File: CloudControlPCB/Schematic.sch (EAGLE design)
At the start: 19 parts, among them J1 AUDIO_JACK_TRRSSMD_RA, U1 LPC4088FBD208, U2 SGTL5000XNLA3R2, X1 PHB_1MM27_2X05_SNT

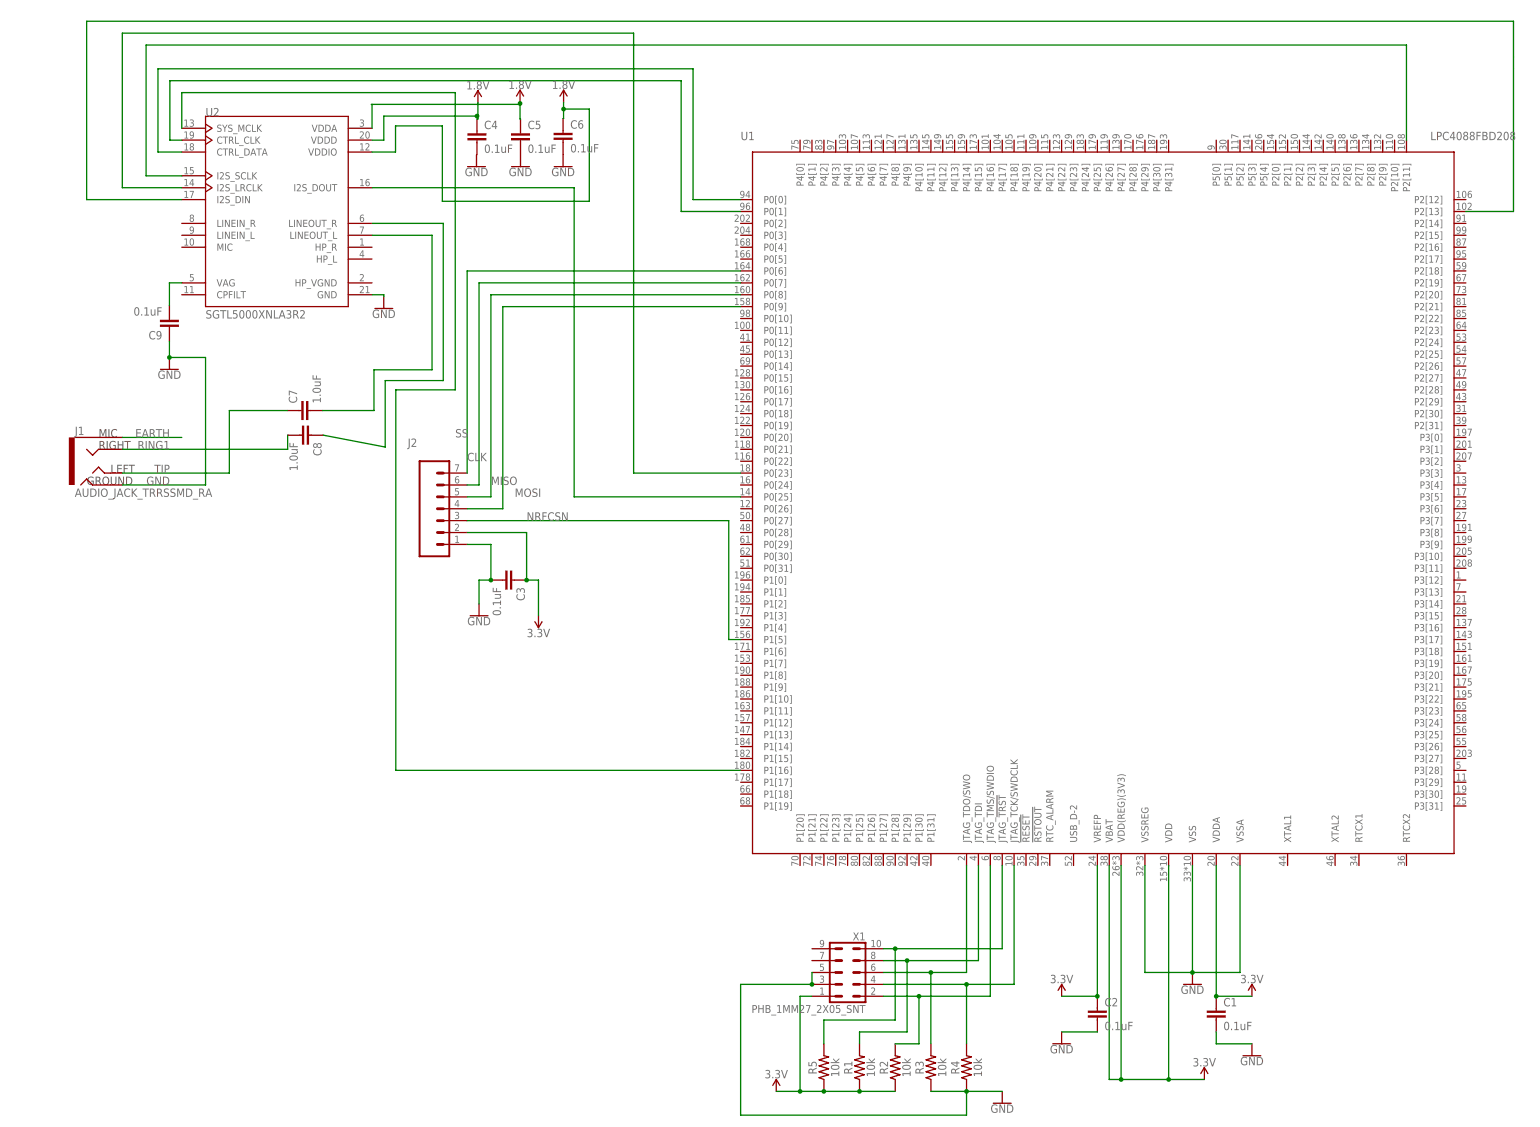
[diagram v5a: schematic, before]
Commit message: Fixed some wiring on the DAC
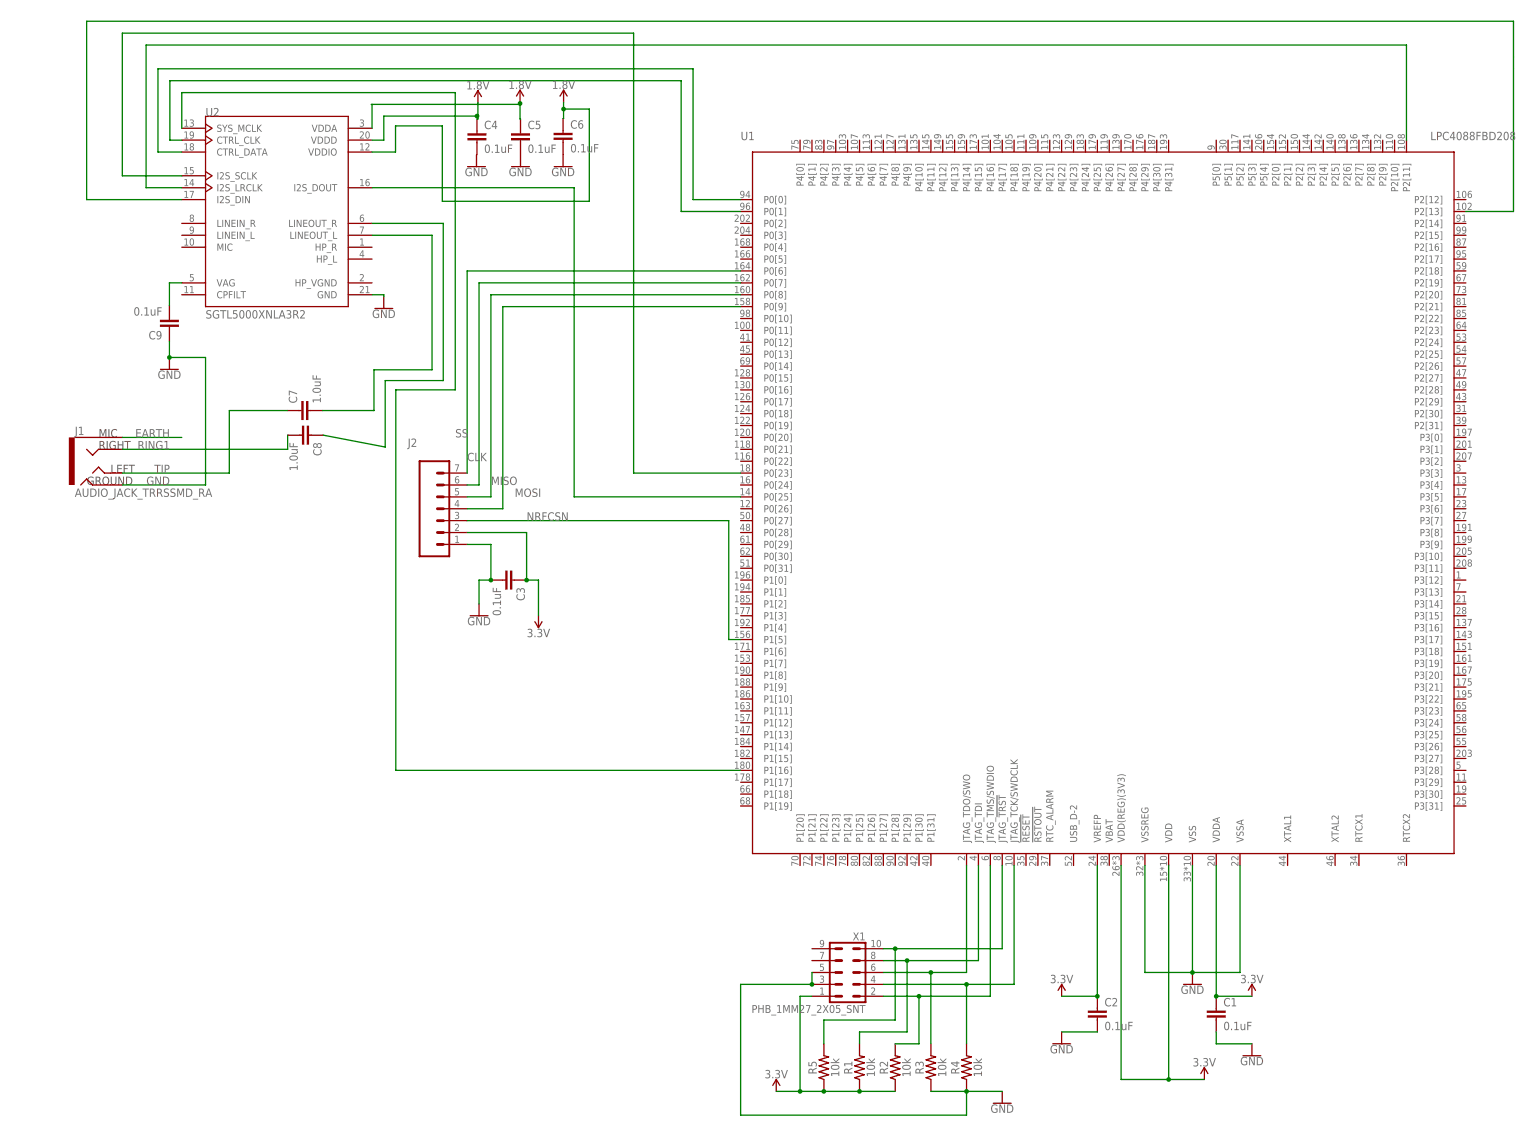
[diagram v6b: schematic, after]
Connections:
- net 3.3V: no longer U1.VBAT
- net N$10: now also U2.I2S_LRCLK; no longer U2.I2S_SCLK
- net N$11: now also U2.I2S_SCLK; no longer U2.I2S_LRCLK

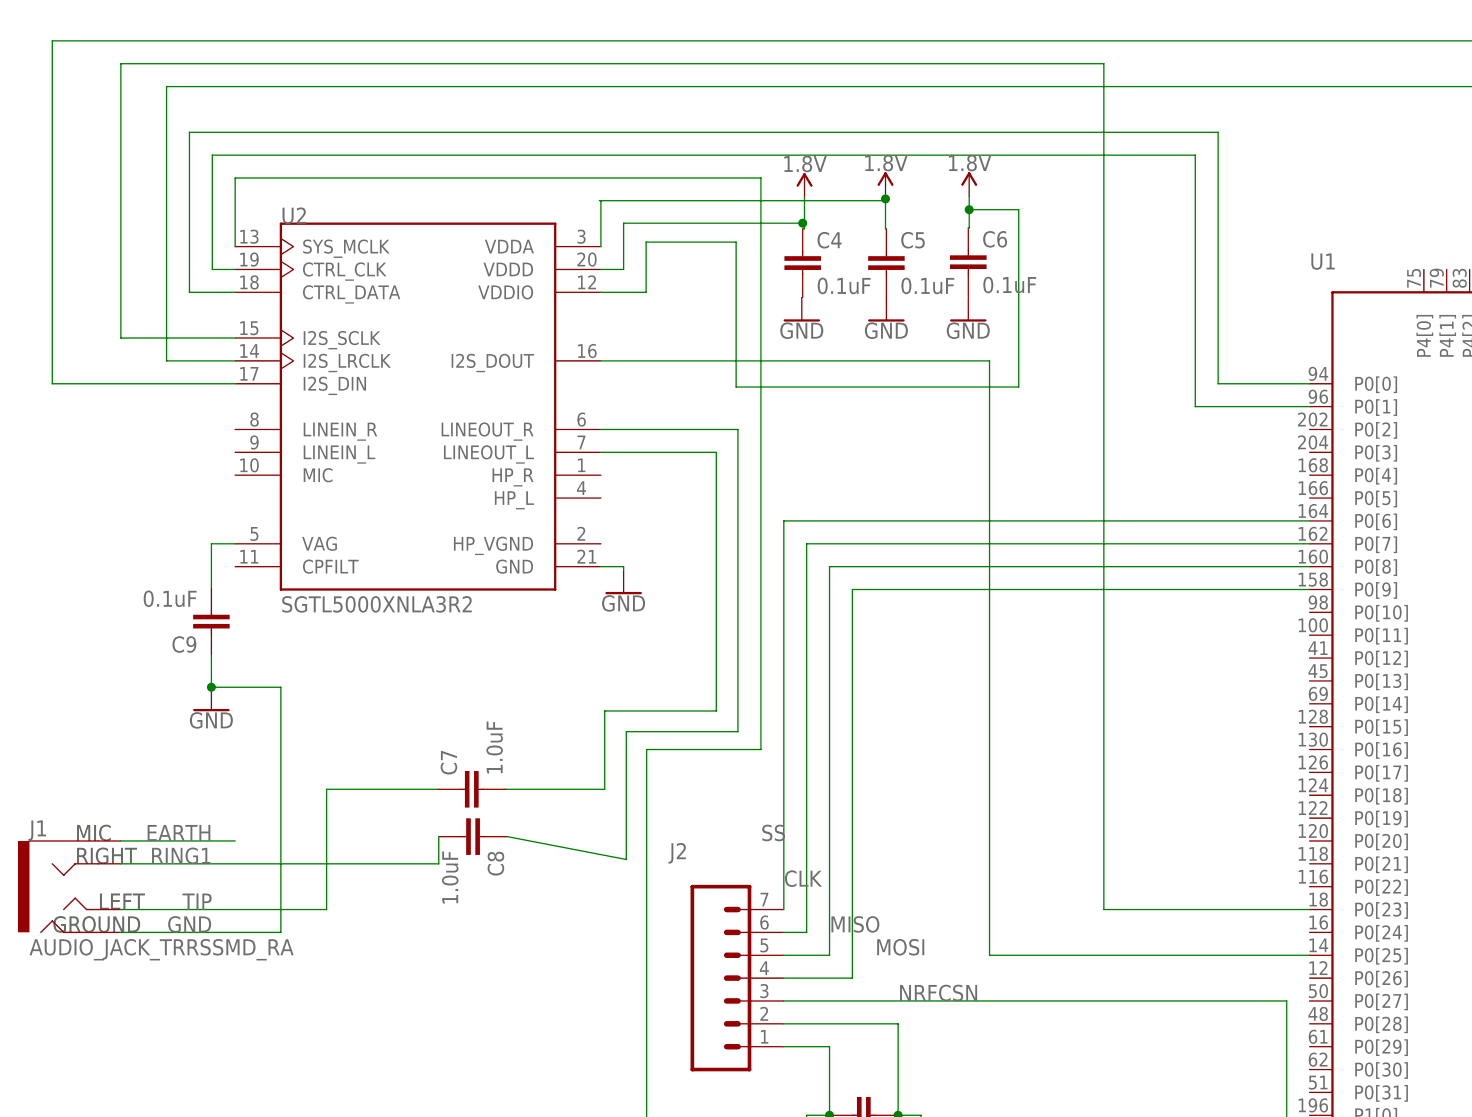
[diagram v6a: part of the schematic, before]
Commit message: Fixed DAC Wiring
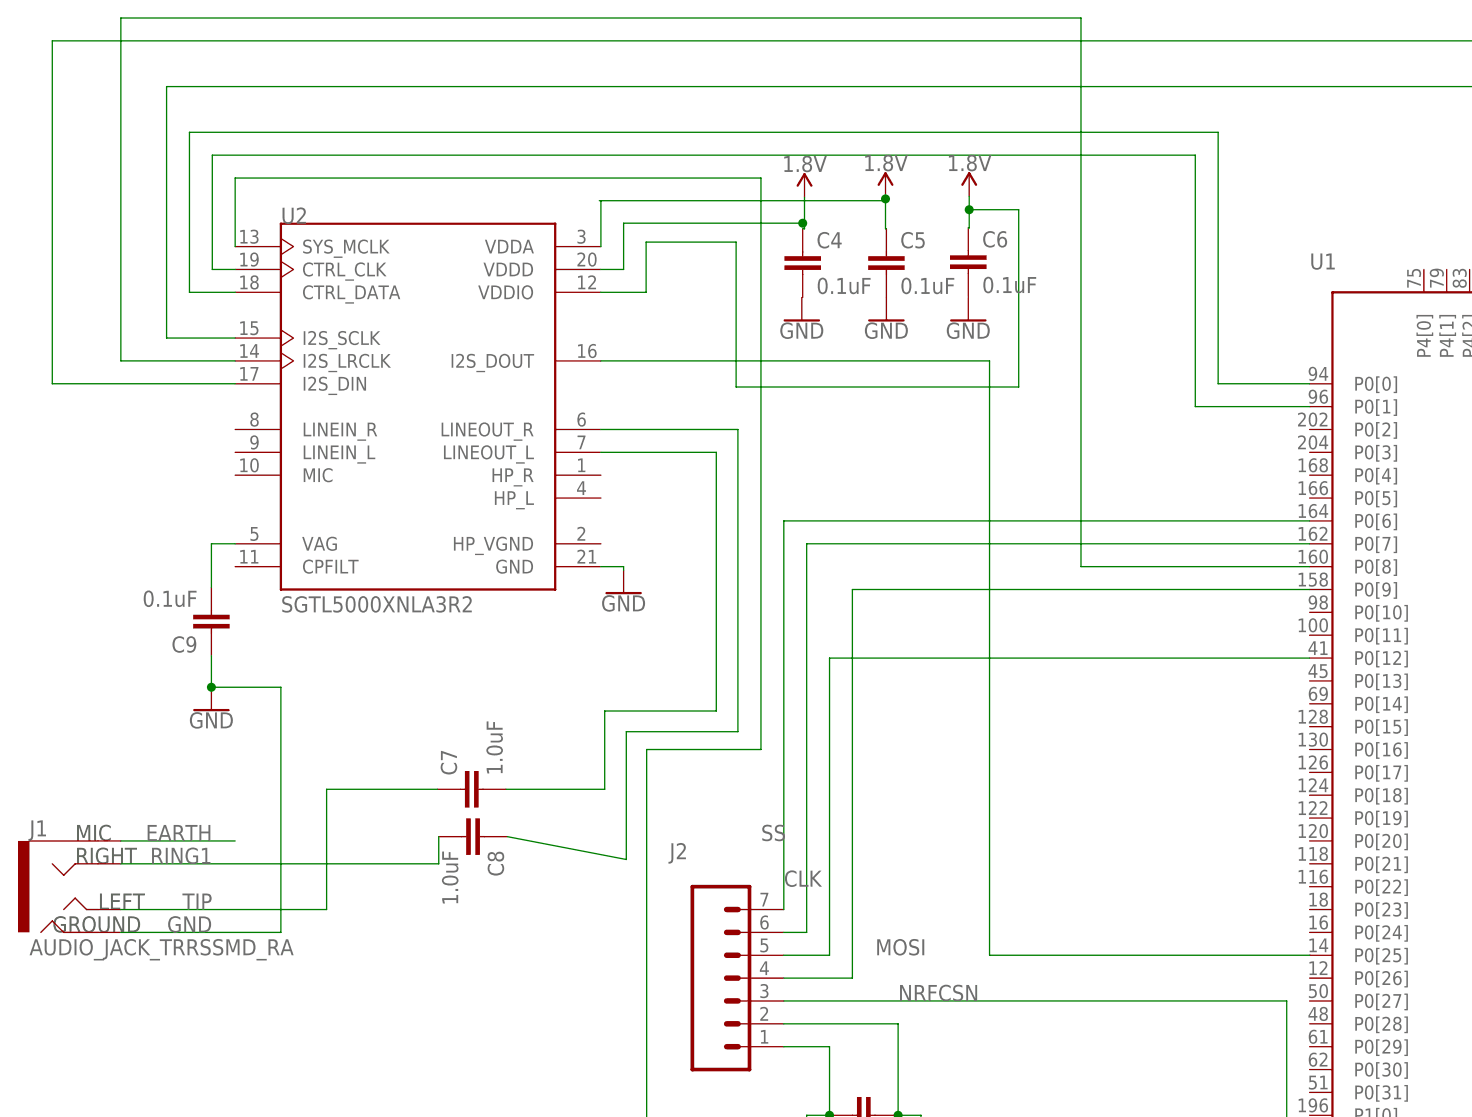
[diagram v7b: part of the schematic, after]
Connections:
- removed net MISO: J2.5, U1.P0[8]
- new net N$17: J2.5, U1.P0[12]
- net N$10: now also U2.I2S_SCLK; no longer U2.I2S_LRCLK
- net N$11: now also U1.P0[8], U2.I2S_LRCLK; no longer U1.P0[23], U2.I2S_SCLK
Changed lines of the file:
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@@
-</segment>
-</net>
-<net name="MISO" class="0">
-<segment>
-<pinref part="U1" gate="G$1" pin="P0[8]"/>
-<wire x1="-5.08" y1="78.74" x2="-58.42" y2="78.74" width="0.1524" layer="91"/>
-<wire x1="-58.42" y1="78.74" x2="-58.42" y2="35.56" width="0.1524" layer="91"/>
-<pinref part="J2" gate="G$1" pin="5"/>
-<wire x1="-58.42" y1="35.56" x2="-63.5" y2="35.56" width="0.1524" layer="91"/>
-<label x="-58.42" y="38.1" size="1.778" layer="95"/>
 </segment>
 </net>
@@
 <net name="N$10" class="0">
 <segment>
-<wire x1="-132.08" y1="101.6" x2="-132.08" y2="132.08" width="0.1524" layer="91"/>
 <pinref part="U1" gate="G$1" pin="P2[11]"/>
 <wire x1="-132.08" y1="132.08" x2="137.16" y2="132.08" width="0.1524" layer="91"/>
 <wire x1="137.16" y1="132.08" x2="137.16" y2="111.76" width="0.1524" layer="91"/>
-<pinref part="U2" gate="G$1" pin="I2S_LRCLK"/>
-<wire x1="-132.08" y1="101.6" x2="-124.46" y2="101.6" width="0.1524" layer="91"/>
-</segment>
-</net>
-<net name="N$11" class="0">
-<segment>
-<pinref part="U1" gate="G$1" pin="P0[23]"/>
-<wire x1="-5.08" y1="40.64" x2="-27.94" y2="40.64" width="0.1524" layer="91"/>
-<wire x1="-27.94" y1="40.64" x2="-27.94" y2="134.62" width="0.1524" layer="91"/>
-<wire x1="-27.94" y1="134.62" x2="-137.16" y2="134.62" width="0.1524" layer="91"/>
-<wire x1="-137.16" y1="134.62" x2="-137.16" y2="104.14" width="0.1524" layer="91"/>
+<wire x1="-132.08" y1="132.08" x2="-132.08" y2="104.14" width="0.1524" layer="91"/>
 <pinref part="U2" gate="G$1" pin="I2S_SCLK"/>
-<wire x1="-137.16" y1="104.14" x2="-124.46" y2="104.14" width="0.1524" layer="91"/>
+<wire x1="-132.08" y1="104.14" x2="-124.46" y2="104.14" width="0.1524" layer="91"/>
 </segment>
 </net>
@@
 </segment>
 </net>
+<net name="N$11" class="0">
+<segment>
+<pinref part="U1" gate="G$1" pin="P0[8]"/>
+<wire x1="-5.08" y1="78.74" x2="-30.48" y2="78.74" width="0.1524" layer="91"/>
+<wire x1="-30.48" y1="78.74" x2="-30.48" y2="139.7" width="0.1524" layer="91"/>
+<wire x1="-30.48" y1="139.7" x2="-137.16" y2="139.7" width="0.1524" layer="91"/>
+<wire x1="-137.16" y1="139.7" x2="-137.16" y2="101.6" width="0.1524" layer="91"/>
+<pinref part="U2" gate="G$1" pin="I2S_LRCLK"/>
+<wire x1="-137.16" y1="101.6" x2="-124.46" y2="101.6" width="0.1524" layer="91"/>
+</segment>
+</net>
+<net name="N$17" class="0">
+<segment>
+<pinref part="U1" gate="G$1" pin="P0[12]"/>
+<wire x1="-5.08" y1="68.58" x2="-58.42" y2="68.58" width="0.1524" layer="91"/>
+<wire x1="-58.42" y1="68.58" x2="-58.42" y2="35.56" width="0.1524" layer="91"/>
+<pinref part="J2" gate="G$1" pin="5"/>
+<wire x1="-58.42" y1="35.56" x2="-63.5" y2="35.56" width="0.1524" layer="91"/>
+</segment>
+</net>

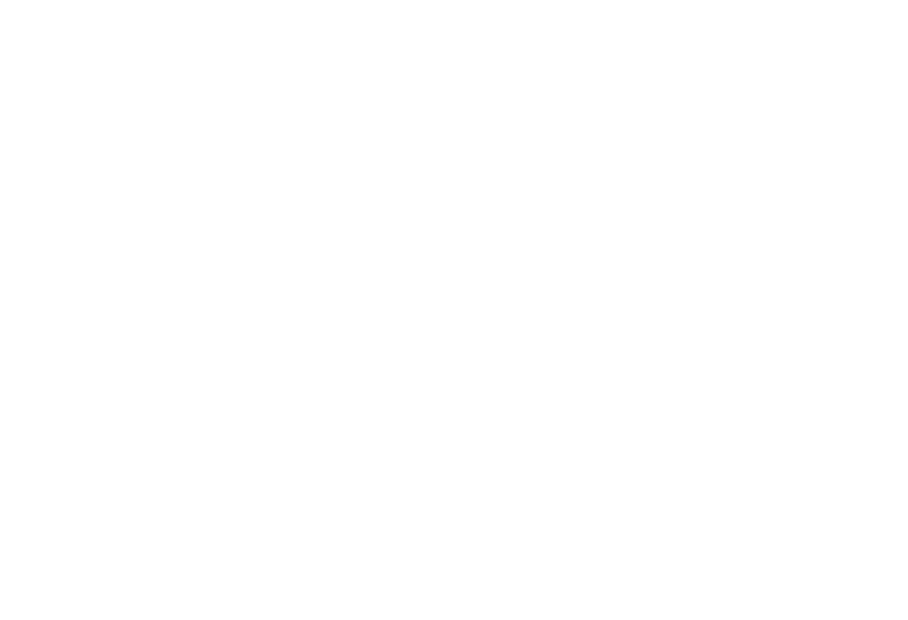
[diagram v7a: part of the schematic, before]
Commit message: Add small regulator circuit (Hopefully no merging issues)
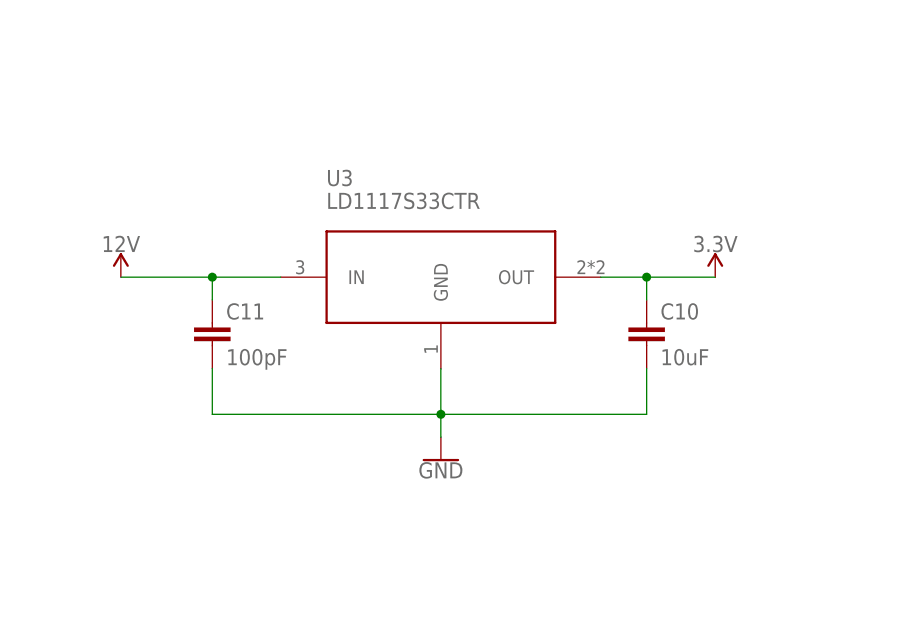
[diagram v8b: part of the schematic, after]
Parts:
- added C10: 10uF, SparkFun-Capacitors:10UF-0603-6.3V-20%
- added C11: 100pF, SparkFun-Capacitors:100PF-0603-50V-5%
- added U3: LD1117S33CTR, LD1117S33CTR:LD1117S33CTR
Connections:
- new net 12V: C11.1, U3.IN
- net 3.3V: now also C10.1, U3.OUT
- net GND: now also C10.2, C11.2, U3.GND
